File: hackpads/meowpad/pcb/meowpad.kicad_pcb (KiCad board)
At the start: 2 copper layers, 110 x 65.5 mm, 16 parts, among them J1 OLED_DISPLAY, SW1 SW_Push_45deg, SW2 SW_Push_45deg, SW3 SW_Push_45deg, SW4 SW_Push_45deg, SW6 SW_Push_45deg, U2 XIAO-RP2040-DIP

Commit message: oops i forgot to put xiao here
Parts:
- U2: value XIAO-RP2040-DIP -> XIAO HERE!!
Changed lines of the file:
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@@
 			)
 		)
-		(property "Value" "XIAO-RP2040-DIP"
+		(property "Value" "XIAO HERE!!"
 			(at 0 0 0)
 			(unlocked yes)

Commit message: small edits
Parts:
- moved U2 0.38 mm to (196.1, 100.5)
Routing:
- net GND: track 91.5 -> 89.5 mm
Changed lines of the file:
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@@
 	(footprint "Seeed Studio XIAO Series Library:XIAO-RP2040-DIP"
 		(layer "F.Cu")
-		(at 196.5 100.5)
+		(at 196.12 100.54)
 		(property "Reference" "U2"
 			(at -8.5 -12 0)
@@
 	)
 	(segment
-		(start 204.665 95.42)
-		(end 204.665 95.665)
-		(width 0.5)
-		(layer "F.Cu")
-		(net 1)
-	)
-	(segment
 		(start 191.5 116.5)
 		(end 195 113)
@@
 	)
 	(segment
-		(start 204.42 95.42)
-		(end 204.665 95.42)
-		(width 0.5)
-		(layer "F.Cu")
-		(net 1)
-	)
-	(segment
 		(start 189.5 81.5)
 		(end 203.42 95.42)
@@
 	)
 	(segment
-		(start 204.665 95.665)
-		(end 204.42 95.42)
-		(width 0.5)
-		(layer "F.Cu")
-		(net 1)
-	)
-	(segment
 		(start 185.92 81.5)
 		(end 189.5 81.5)
@@
 		(end 177 116.5)
 		(width 0.5)
-		(layer "F.Cu")
-		(net 1)
-	)
-	(segment
-		(start 203.42 95.42)
-		(end 204.665 95.42)
-		(width 0.2)
 		(layer "F.Cu")
 		(net 1)
@@
 	)
 	(segment
+		(start 202.58 95.42)
+		(end 199.5 98.5)
+		(width 0.5)
+		(layer "B.Cu")
+		(net 1)
+	)
+	(segment
+		(start 204.665 95.42)
+		(end 202.58 95.42)
+		(width 0.5)
+		(layer "B.Cu")
+		(net 1)
+	)
+	(segment
 		(start 199.5 98.5)
-		(end 202.58 95.42)
-		(width 0.5)
-		(layer "B.Cu")
-		(net 1)
-	)
-	(segment
-		(start 202.58 95.42)
-		(end 204.665 95.42)
-		(width 0.5)
-		(layer "B.Cu")
-		(net 1)
-	)
-	(segment
-		(start 199.5 108.5)
-		(end 199.5 98.5)
-		(width 0.5)
-		(layer "B.Cu")
-		(net 1)
-	)
-	(segment
-		(start 195 113)
 		(end 199.5 108.5)
 		(width 0.5)
@@
 		(layer "B.Cu")
 		(net 1)
+	)
+	(segment
+		(start 199.5 108.5)
+		(end 195 113)
+		(width 0.5)
+		(layer "B.Cu")
+		(net 1)

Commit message: updates
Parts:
- moved U2 5.14 mm to (201.2, 100.0), turned to -90 degrees
- moved J1 2.06 mm to (173.6, 110.4)
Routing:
- net SLIDER: track 98.7 -> 164.3 mm, vias 2 -> 0
- net ROTARYB: track 88.9 -> 54.3 mm, vias 2 -> 0
- net ROW1: track 138.8 -> 117.0 mm, vias 2 -> 0
- net COL1: track 72.0 -> 91.2 mm, vias 1 -> 2
- net COL2: track 95.9 -> 112.4 mm
- net ROTARYA: track 76.0 -> 59.6 mm
- net COL3: track 38.9 -> 53.8 mm, vias 1 -> 0
- net ROW2: track 102.4 -> 87.7 mm, vias 2 -> 0
- net VCC: track 34.5 -> 47.3 mm
- net SCL: track 37.2 -> 24.8 mm, vias 1 -> 0
- net SDA: track 33.0 -> 24.8 mm, vias 1 -> 0
- net Net-(C1-Pad1): track 43.6 -> 48.0 mm
- net GND: track 89.5 -> 88.1 mm, vias 2 -> 0
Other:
- board size 110 x 65.5 mm -> 109.5 x 65.5 mm

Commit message: gerbers
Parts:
- added NYA: LOGO, Documents:catgirl, F.Cu at (142.0, 97.5)
- U2: value XIAO HERE!! -> XIAO-RP2040-DIP
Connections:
- U2 pad 12: unconnected-(U2-3V3-Pad12) -> +3.3V
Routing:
- net +3.3V: track 0.00 -> 101.9 mm

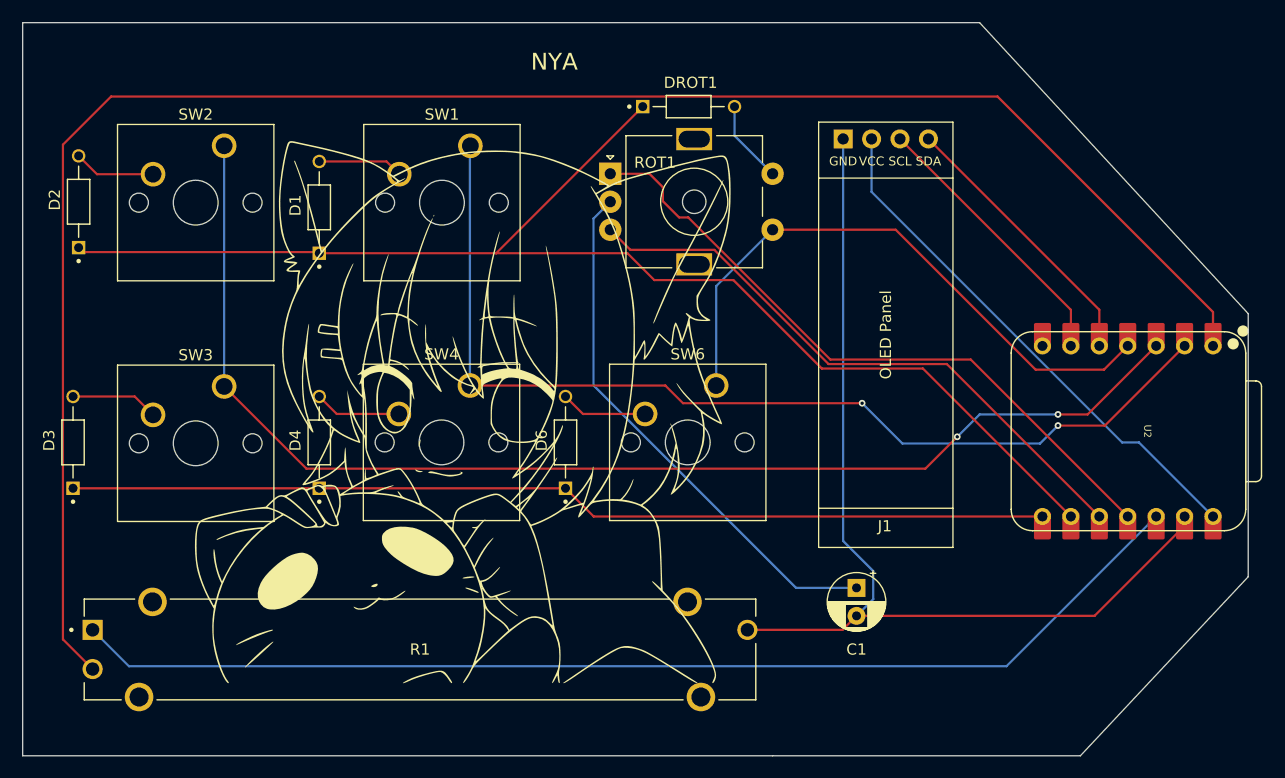
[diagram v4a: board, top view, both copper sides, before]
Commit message: redesigned pcb
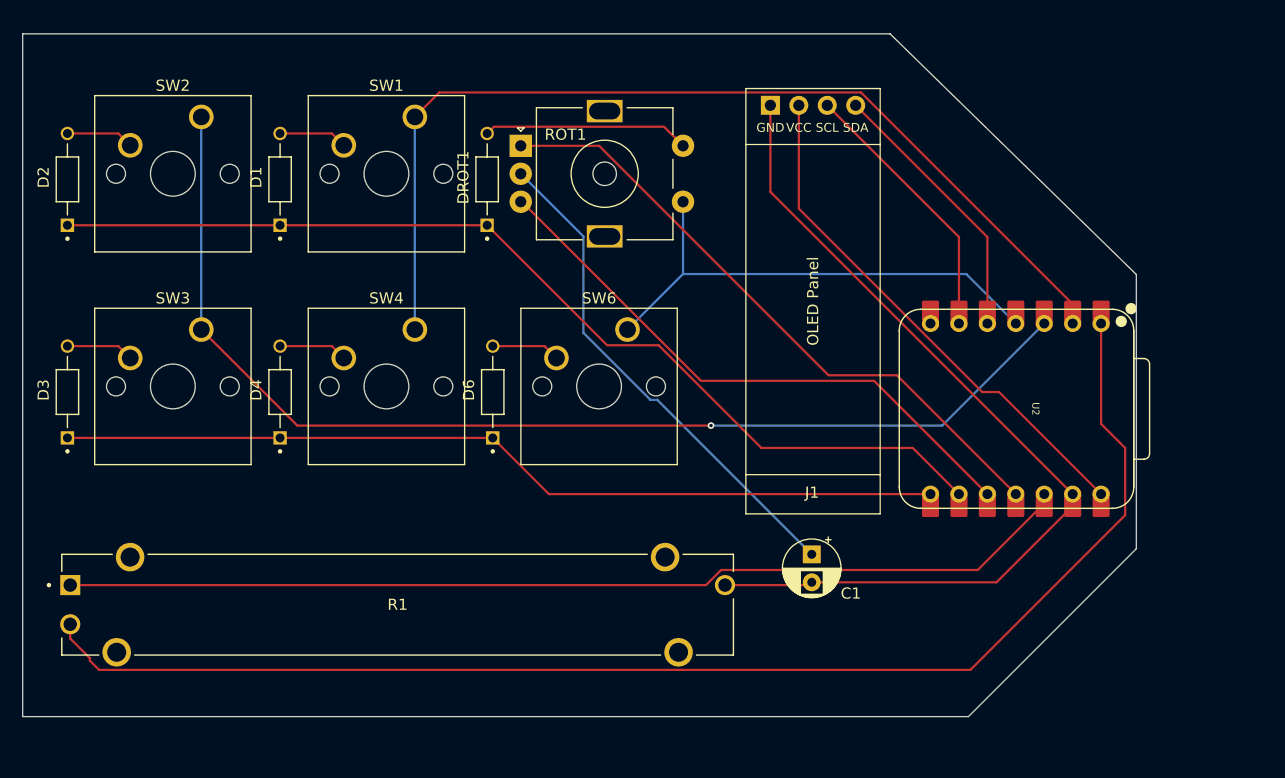
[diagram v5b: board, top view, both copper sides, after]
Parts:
- NYA: moved to B.Cu
- moved DROT1 19.1 mm to (144.0, 77.5), turned to 90 degrees
- moved U2 10.2 mm to (191.2, 98.0)
- moved SW6 9.37 mm to (156.5, 90.9)
- moved NYA 8.51 mm to (150.5, 98.0), turned to 180 degrees
- moved ROT1 8.38 mm to (147.0, 74.5)
- moved D6 7.91 mm to (144.5, 96.5)
- moved J1 7.16 mm to (167.1, 107.4)
- moved SW4 7.01 mm to (137.5, 90.9)
- moved D4 5.70 mm to (125.5, 96.5)
- moved SW1 5.59 mm to (137.5, 71.9)
- moved SW3 5.47 mm to (118.5, 90.9)
- moved C1 5.00 mm to (173.0, 111.0)
- moved D3 4.53 mm to (106.5, 96.5)
- moved R1 4.47 mm to (136.0, 115.5)
- moved D1 4.30 mm to (125.5, 77.5)
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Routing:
- net SLIDER: track 164.3 -> 120.6 mm
- net ROW1: track 117.0 -> 89.6 mm
- net ROTARYS2: track 7.41 -> 18.5 mm
- net +3.3V: track 101.9 -> 90.9 mm
- net COL2: track 112.4 -> 101.6 mm, vias 2 -> 1
- net COL3: track 53.8 -> 45.0 mm
- net ROW2: track 87.7 -> 79.2 mm
- net GND: track 88.1 -> 81.0 mm
- net COL1: track 91.2 -> 88.2 mm, vias 2 -> 0
- net Net-(C1-Pad1): track 48.0 -> 45.1 mm
- net ROTARYA: track 59.6 -> 57.1 mm
- net ROTARYB: track 54.3 -> 52.5 mm
- net Net-(D3-PadA): track 7.83 -> 6.05 mm
- net Net-(D6-PadA): track 7.76 -> 6.13 mm
- net Net-(D4-PadA): track 7.76 -> 6.13 mm
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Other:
- board size 109.5 x 65.5 mm -> 99.5 x 61 mm
